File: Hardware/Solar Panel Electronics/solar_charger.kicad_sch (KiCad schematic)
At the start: 20 parts

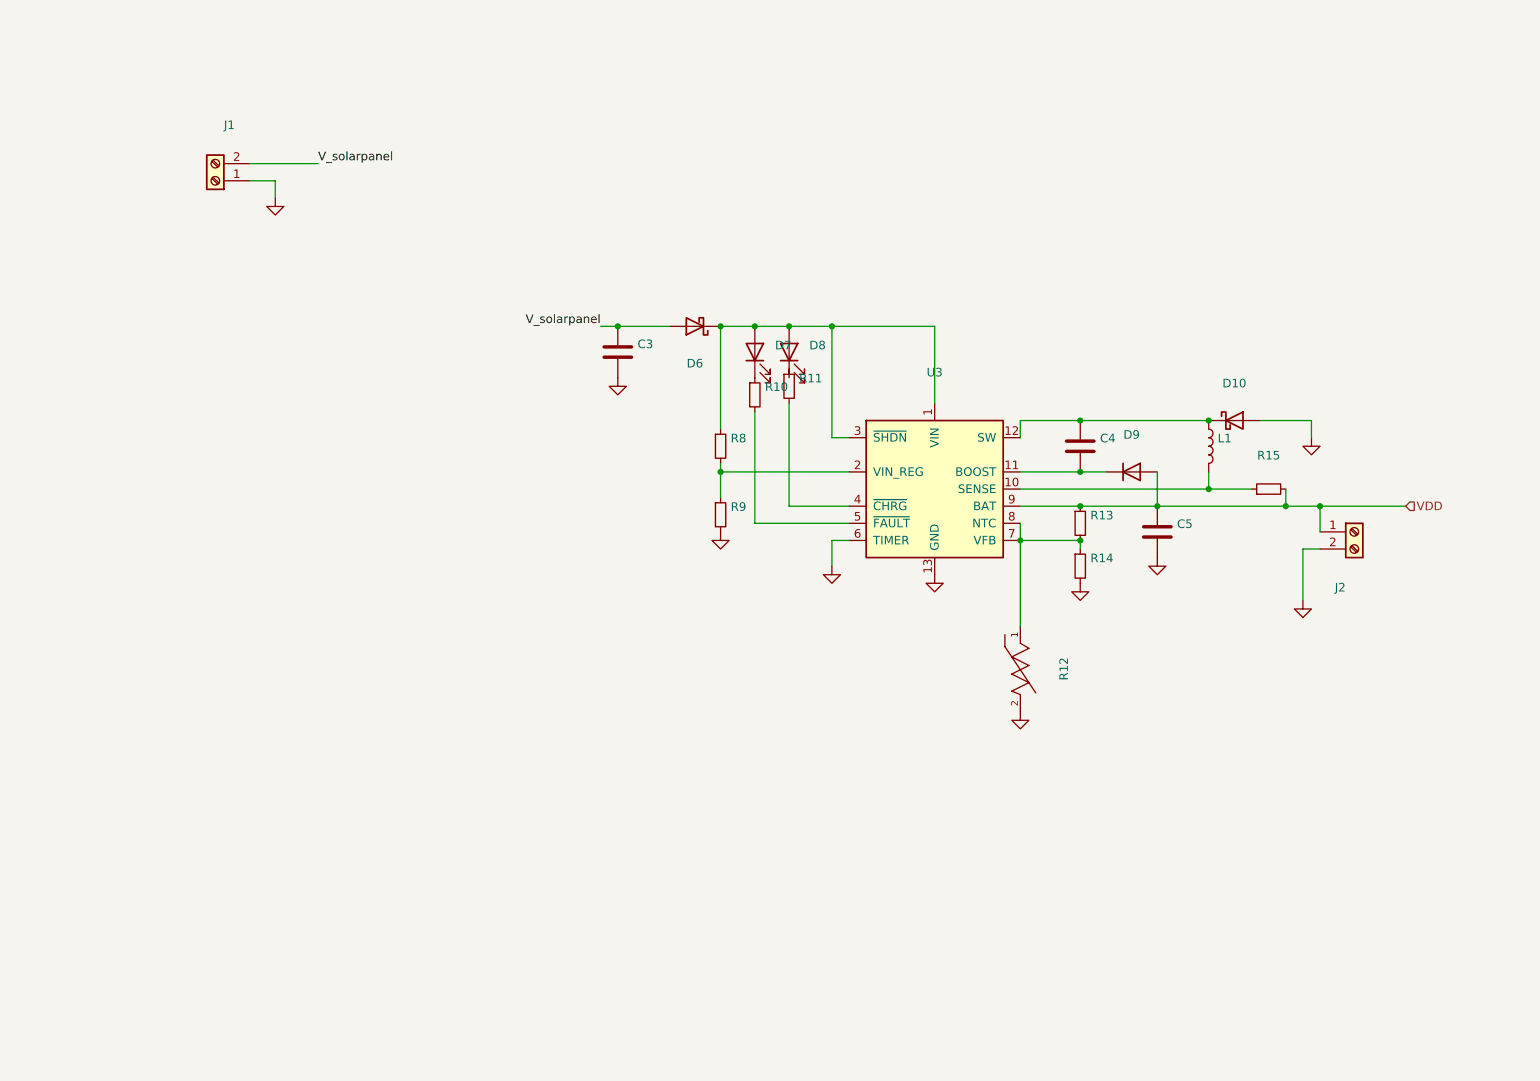
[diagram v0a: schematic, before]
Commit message: Move uart to separate sheet and fix
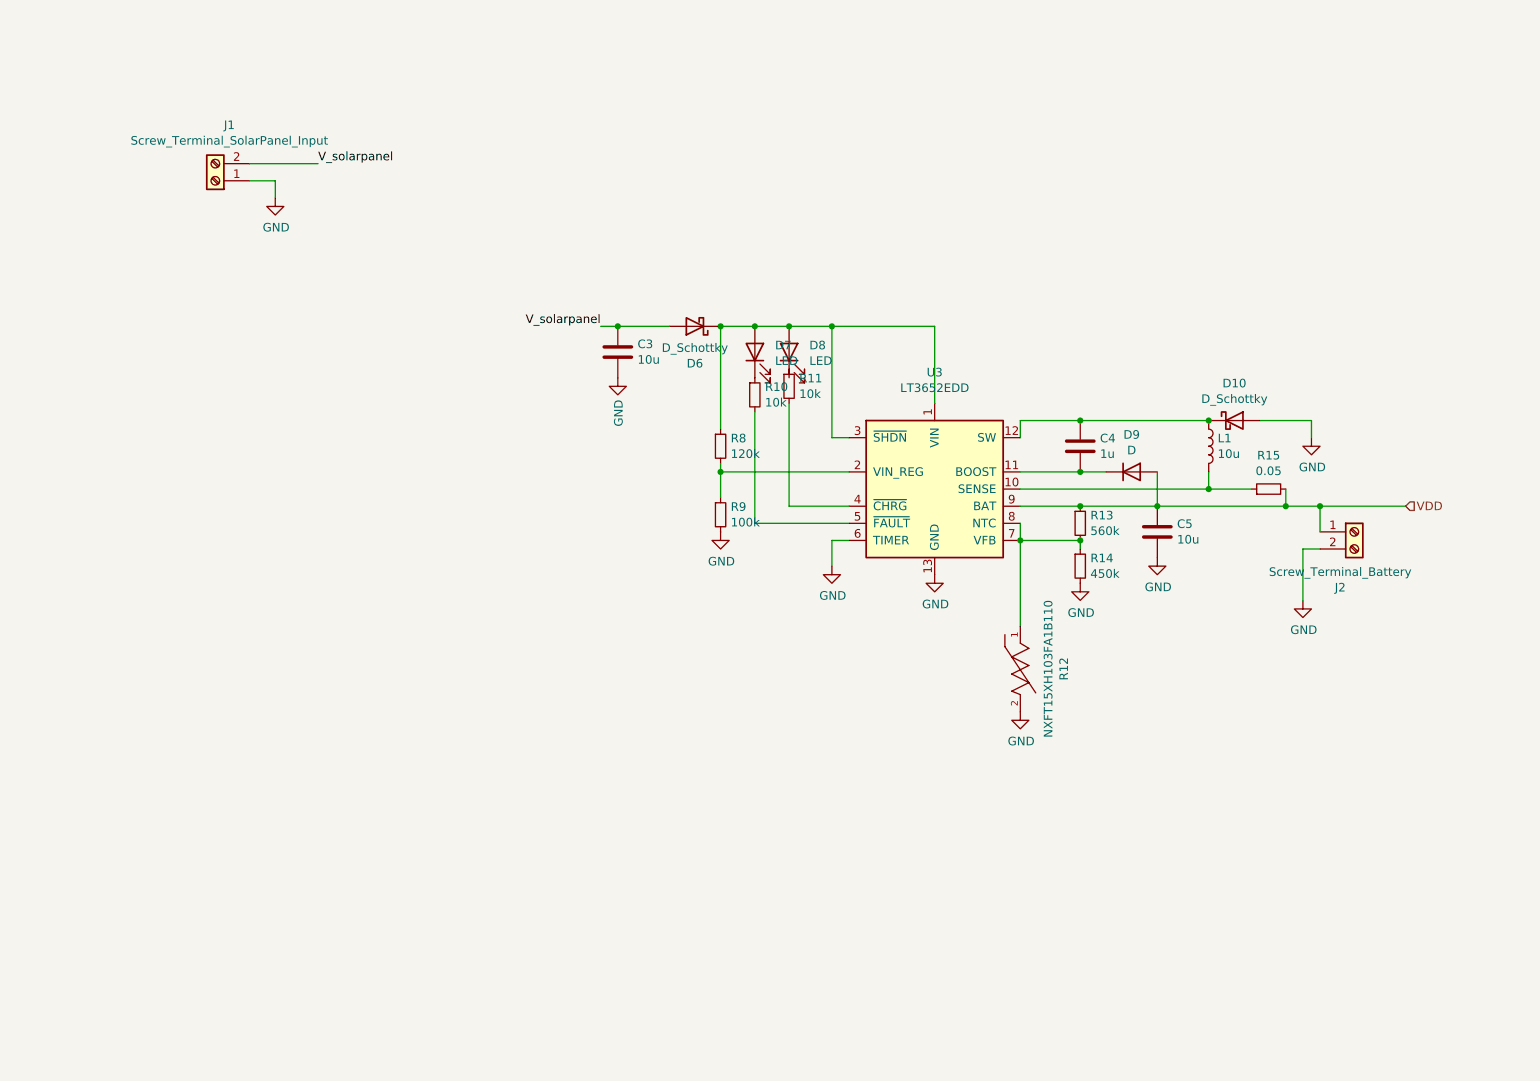
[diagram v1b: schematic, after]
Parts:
- C3, C5, L1: value (none) -> 10u
- C4: value (none) -> 1u
- D10, D6: value (none) -> D_Schottky
- D7, D8: value (none) -> LED
- D9: value (none) -> D
- J1: value (none) -> Screw_Terminal_SolarPanel_Input
- J2: value (none) -> Screw_Terminal_Battery
- R10, R11: value (none) -> 10k
- R12: value (none) -> NXFT15XH103FA1B110; footprint (none) -> Murata_Electronics_North_America-NXF_151B110-0-0-*
- R13: value (none) -> 560k
- R14: value (none) -> 450k
- R15: value (none) -> 0.05
- R8: value (none) -> 120k
- R9: value (none) -> 100k
- U3: value (none) -> LT3652EDD; footprint (none) -> Package_DFN_QFN:DFN-12-1EP_3x3mm_P0.45mm_EP1.66x2.38mm
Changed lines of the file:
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@@
     (in_bom yes) (on_board yes)
     (property "Reference" "U3" (id 0) (at 151.13 67.7926 0))
-    (property "Value" "" (id 1) (at 151.13 70.104 0))
-    (property "Footprint" "" (id 2) (at 151.13 100.33 0)
+    (property "Value" "LT3652EDD" (id 1) (at 151.13 70.104 0))
+    (property "Footprint" "Package_DFN_QFN:DFN-12-1EP_3x3mm_P0.45mm_EP1.66x2.38mm" (id 2) (at 151.13 100.33 0)
       (effects (font (size 1.27 1.27)) hide)
     )
@@
     (in_bom yes) (on_board yes)
     (property "Reference" "J1" (id 0) (at 46.5328 31.115 0))
-    (property "Value" "" (id 1) (at 46.5328 33.4264 0))
+    (property "Value" "Screw_Terminal_SolarPanel_Input" (id 1) (at 46.5328 33.4264 0))
     (property "Footprint" "" (id 2) (at 44.45 39.37 0)
       (effects (font (size 1.27 1.27)) hide)
@@
       (effects (font (size 1.27 1.27)) hide)
     )
-    (property "Value" "" (id 1) (at 53.467 46.3042 0))
+    (property "Value" "GND" (id 1) (at 53.467 46.3042 0))
     (property "Footprint" "" (id 2) (at 53.34 41.91 0)
       (effects (font (size 1.27 1.27)) hide)
@@
       (effects (font (size 1.27 1.27)) hide)
     )
-    (property "Value" "" (id 1) (at 151.257 102.1842 0))
+    (property "Value" "GND" (id 1) (at 151.257 102.1842 0))
     (property "Footprint" "" (id 2) (at 151.13 97.79 0)
       (effects (font (size 1.27 1.27)) hide)
@@
       (effects (font (size 1.27 1.27)) (justify left))
     )
-    (property "Value" "" (id 1) (at 120.8786 79.883 0)
+    (property "Value" "120k" (id 1) (at 120.8786 79.883 0)
       (effects (font (size 1.27 1.27)) (justify left))
     )
@@
       (effects (font (size 1.27 1.27)) (justify left))
     )
-    (property "Value" "" (id 1) (at 120.8786 90.043 0)
+    (property "Value" "100k" (id 1) (at 120.8786 90.043 0)
       (effects (font (size 1.27 1.27)) (justify left))
     )
@@
       (effects (font (size 1.27 1.27)) (justify right))
     )
-    (property "Value" "" (id 1) (at 107.061 65.913 0)
+    (property "Value" "10u" (id 1) (at 107.061 65.913 0)
       (effects (font (size 1.27 1.27)) (justify right))
     )
@@
       (effects (font (size 1.27 1.27)) (justify left))
     )
-    (property "Value" "" (id 1) (at 125.9586 72.263 0)
+    (property "Value" "10k" (id 1) (at 125.9586 72.263 0)
       (effects (font (size 1.27 1.27)) (justify left))
     )
@@
       (effects (font (size 1.27 1.27)) hide)
     )
-    (property "Value" "" (id 1) (at 104.267 71.8312 90)
+    (property "Value" "GND" (id 1) (at 104.267 71.8312 90)
       (effects (font (size 1.27 1.27)) (justify right))
     )
@@
       (effects (font (size 1.27 1.27)) (justify right))
     )
-    (property "Value" "" (id 1) (at 127.4572 66.0908 90)
+    (property "Value" "LED" (id 1) (at 127.4572 66.0908 90)
       (effects (font (size 1.27 1.27)) (justify right))
     )
@@
       (effects (font (size 1.27 1.27)) (justify left))
     )
-    (property "Value" "" (id 1) (at 131.0386 70.993 0)
+    (property "Value" "10k" (id 1) (at 131.0386 70.993 0)
       (effects (font (size 1.27 1.27)) (justify left))
     )
@@
       (effects (font (size 1.27 1.27)) (justify right))
     )
-    (property "Value" "" (id 1) (at 132.5372 66.0908 90)
+    (property "Value" "LED" (id 1) (at 132.5372 66.0908 90)
       (effects (font (size 1.27 1.27)) (justify right))
     )
@@
       (effects (font (size 1.27 1.27)) hide)
     )
-    (property "Value" "" (id 1) (at 119.507 95.8342 0))
+    (property "Value" "GND" (id 1) (at 119.507 95.8342 0))
     (property "Footprint" "" (id 2) (at 119.38 91.44 0)
       (effects (font (size 1.27 1.27)) hide)
@@
       (effects (font (size 1.27 1.27)) hide)
     )
-    (property "Value" "" (id 1) (at 136.017 100.9142 0))
+    (property "Value" "GND" (id 1) (at 136.017 100.9142 0))
     (property "Footprint" "" (id 2) (at 135.89 96.52 0)
       (effects (font (size 1.27 1.27)) hide)
@@
       (effects (font (size 1.27 1.27)) (justify left))
     )
-    (property "Value" "" (id 1) (at 174.2186 91.313 0)
+    (property "Value" "560k" (id 1) (at 174.2186 91.313 0)
       (effects (font (size 1.27 1.27)) (justify left))
     )
@@
       (effects (font (size 1.27 1.27)) (justify left))
     )
-    (property "Value" "" (id 1) (at 174.2186 97.663 0)
+    (property "Value" "450k" (id 1) (at 174.2186 97.663 0)
       (effects (font (size 1.27 1.27)) (justify left))
     )
@@
       (effects (font (size 1.27 1.27)) hide)
     )
-    (property "Value" "" (id 1) (at 172.847 103.4542 0))
+    (property "Value" "GND" (id 1) (at 172.847 103.4542 0))
     (property "Footprint" "" (id 2) (at 172.72 99.06 0)
       (effects (font (size 1.27 1.27)) hide)
@@
     (in_bom yes) (on_board yes)
     (property "Reference" "R12" (id 0) (at 170.307 111.76 0))
-    (property "Value" "" (id 1) (at 167.9956 111.76 0))
-    (property "Footprint" "" (id 2) (at 173.99 102.87 0)
+    (property "Value" "NXFT15XH103FA1B110" (id 1) (at 167.9956 111.76 0))
+    (property "Footprint" "Murata_Electronics_North_America-NXF_151B110-0-0-*" (id 2) (at 173.99 102.87 0)
       (effects (font (size 1.27 1.27)) (justify left) hide)
     )
@@
       (effects (font (size 1.27 1.27)) hide)
     )
-    (property "Value" "" (id 1) (at 163.957 122.5042 0))
+    (property "Value" "GND" (id 1) (at 163.957 122.5042 0))
     (property "Footprint" "" (id 2) (at 163.83 118.11 0)
       (effects (font (size 1.27 1.27)) hide)
@@
       (effects (font (size 1.27 1.27)) (justify right))
     )
-    (property "Value" "" (id 1) (at 187.071 92.583 0)
+    (property "Value" "10u" (id 1) (at 187.071 92.583 0)
       (effects (font (size 1.27 1.27)) (justify right))
     )
@@
       (effects (font (size 1.27 1.27)) hide)
     )
-    (property "Value" "" (id 1) (at 184.277 99.6442 0))
+    (property "Value" "GND" (id 1) (at 184.277 99.6442 0))
     (property "Footprint" "" (id 2) (at 184.15 95.25 0)
       (effects (font (size 1.27 1.27)) hide)
@@
     (in_bom yes) (on_board yes)
     (property "Reference" "R15" (id 0) (at 200.66 80.1116 90))
-    (property "Value" "" (id 1) (at 200.66 82.423 90))
+    (property "Value" "0.05" (id 1) (at 200.66 82.423 90))
     (property "Footprint" "" (id 2) (at 200.66 85.09 0)
       (effects (font (size 1.27 1.27)) hide)
@@
       (effects (font (size 1.27 1.27)) (justify right))
     )
-    (property "Value" "" (id 1) (at 175.641 79.883 0)
+    (property "Value" "1u" (id 1) (at 175.641 79.883 0)
       (effects (font (size 1.27 1.27)) (justify right))
     )
@@
     (in_bom yes) (on_board yes)
     (property "Reference" "D9" (id 0) (at 180.34 77.0382 0))
-    (property "Value" "" (id 1) (at 180.34 79.3496 0))
+    (property "Value" "D" (id 1) (at 180.34 79.3496 0))
     (property "Footprint" "" (id 2) (at 180.34 82.55 0)
       (effects (font (size 1.27 1.27)) hide)
@@
       (effects (font (size 1.27 1.27)) (justify left))
     )
-    (property "Value" "" (id 1) (at 193.0908 79.883 0)
+    (property "Value" "10u" (id 1) (at 193.0908 79.883 0)
       (effects (font (size 1.27 1.27)) (justify left))
     )
@@
     (in_bom yes) (on_board yes)
     (property "Reference" "J2" (id 0) (at 211.2772 99.695 0))
-    (property "Value" "" (id 1) (at 211.2772 97.3836 0))
+    (property "Value" "Screw_Terminal_Battery" (id 1) (at 211.2772 97.3836 0))
     (property "Footprint" "" (id 2) (at 213.36 91.44 0)
       (effects (font (size 1.27 1.27)) hide)
@@
       (effects (font (size 1.27 1.27)) hide)
     )
-    (property "Value" "" (id 1) (at 205.867 105.9942 0))
+    (property "Value" "GND" (id 1) (at 205.867 105.9942 0))
     (property "Footprint" "" (id 2) (at 205.74 101.6 0)
       (effects (font (size 1.27 1.27)) hide)
@@
     (in_bom yes) (on_board yes)
     (property "Reference" "D10" (id 0) (at 195.58 69.4182 0))
-    (property "Value" "" (id 1) (at 195.58 71.7296 0))
+    (property "Value" "D_Schottky" (id 1) (at 195.58 71.7296 0))
     (property "Footprint" "" (id 2) (at 195.58 74.93 0)
       (effects (font (size 1.27 1.27)) hide)
@@
       (effects (font (size 1.27 1.27)) hide)
     )
-    (property "Value" "" (id 1) (at 207.137 81.8642 0))
+    (property "Value" "GND" (id 1) (at 207.137 81.8642 0))
     (property "Footprint" "" (id 2) (at 207.01 77.47 0)
       (effects (font (size 1.27 1.27)) hide)
@@
     (in_bom yes) (on_board yes)
     (property "Reference" "D6" (id 0) (at 115.57 66.4718 0))
-    (property "Value" "" (id 1) (at 115.57 64.1604 0))
+    (property "Value" "D_Schottky" (id 1) (at 115.57 64.1604 0))
     (property "Footprint" "" (id 2) (at 115.57 60.96 0)
       (effects (font (size 1.27 1.27)) hide)

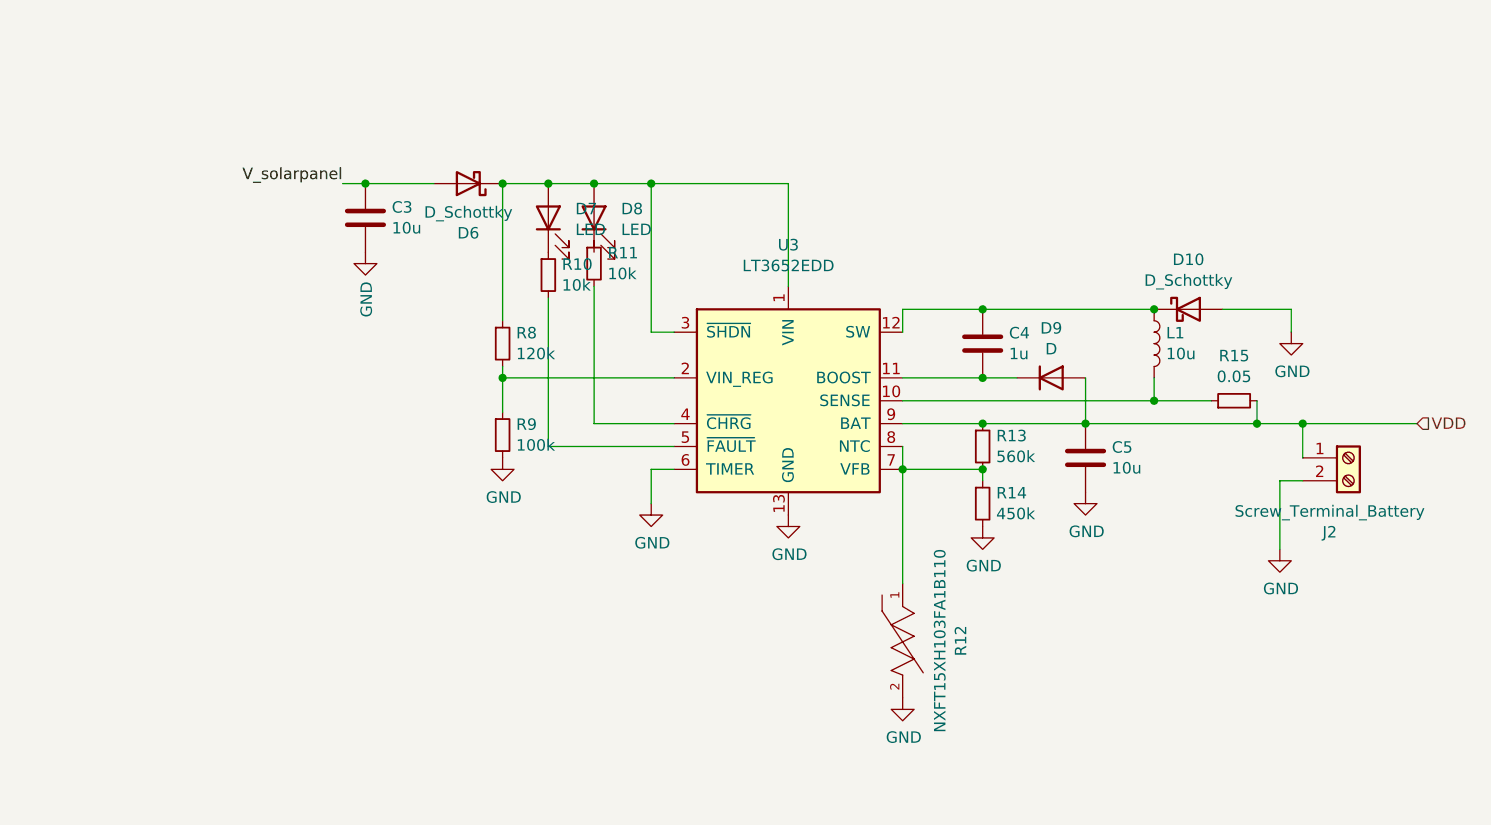
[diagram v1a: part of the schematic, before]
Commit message: Edited the charging circuit, need to resize components
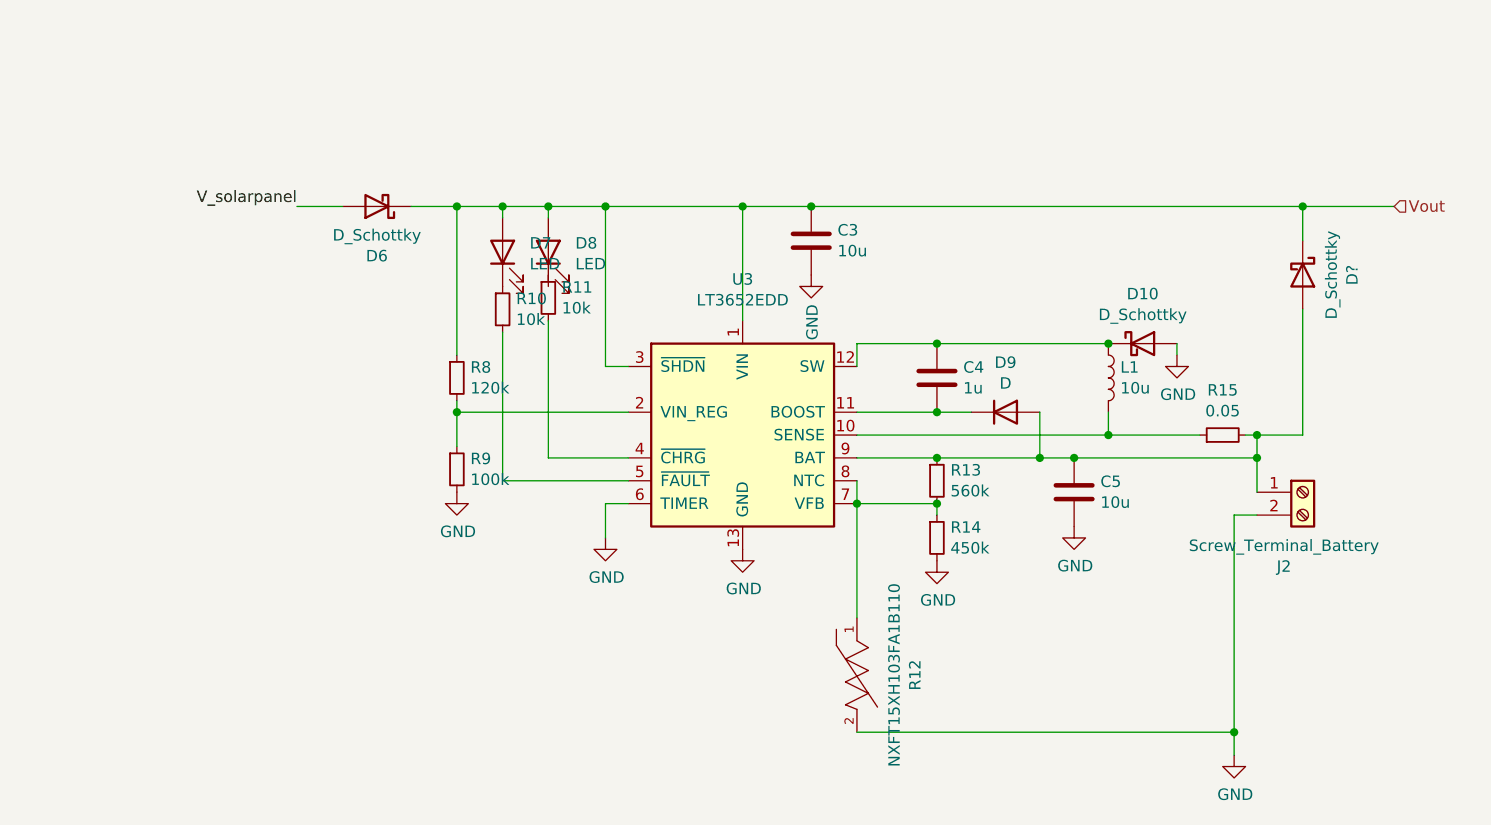
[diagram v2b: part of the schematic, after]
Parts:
- added D?: D_Schottky, symbol Device:D_Schottky
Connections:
- net V_solarpanel: no longer C3.2
- net Vout: now reaches D6.1 (K), D7.2 (A), D8.2 (A), R8.1, U3.1 (VIN), U3.3 (~{SHDN})
- net Vout: now also C3.2, D?.1 (K)
- net VDD: no longer names the net of C5.2, D9.2 (A), J2.1 (Pin_1), R13.1, R15.2, U3.9 (BAT)
- net VDD: now also D?.2 (A)
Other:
- moved on the sheet: C3, C4, C5, D10, D6, D7, D8, D9, J2, L1, R10, R11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
